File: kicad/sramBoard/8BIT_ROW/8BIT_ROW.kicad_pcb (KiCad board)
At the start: 4 copper layers, 64 parts, among them Q1 NMOS, Q10 NMOS, Q11 PMOS, Q12 NMOS, Q13 PMOS, Q14 NMOS, Q15 NMOS, Q16 NMOS, Q17 NMOS, Q18 NMOS, Q19 PMOS, Q2 NMOS, Q20 NMOS, Q21 PMOS, Q22 NMOS, Q23 NMOS, Q24 NMOS, Q25 NMOS, Q26 NMOS, Q27 PMOS, Q28 NMOS, Q29 PMOS, Q3 PMOS, Q30 NMOS, Q31 NMOS, Q32 NMOS, Q33 NMOS, Q34 NMOS, Q35 PMOS, Q36 NMOS, Q37 PMOS, Q38 NMOS, Q39 NMOS, Q4 NMOS, Q40 NMOS, Q41 NMOS, Q42 NMOS, Q43 PMOS, Q44 NMOS, Q45 PMOS, Q46 NMOS, Q47 NMOS, Q48 NMOS, Q49 NMOS, Q5 PMOS, Q50 NMOS, Q51 PMOS, Q52 NMOS, Q53 PMOS, Q54 NMOS, Q55 NMOS, Q56 NMOS, Q57 NMOS, Q58 NMOS, Q59 PMOS, Q6 NMOS, Q60 NMOS, Q61 PMOS, Q62 NMOS, Q63 NMOS, Q64 NMOS, Q7 NMOS, Q8 NMOS, Q9 NMOS

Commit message: added busbars but still some issues
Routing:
- added copper zone on B.Cu, net /BL_{0}
- added copper zone on B.Cu, net /BL_{1}
- added copper zone on B.Cu, net /BL_{2}
- added copper zone on B.Cu, net /BL_{3}
- added copper zone on B.Cu, net /BL_{4}
- added copper zone on B.Cu, net /BL_{5}
- added copper zone on B.Cu, net /BL_{6}
- added copper zone on B.Cu, net /BL_{7}
- added copper zone on B.Cu, net /~{BL_{0}}
- added copper zone on B.Cu, net /~{BL_{1}}
- added copper zone on B.Cu, net /~{BL_{2}}
- added copper zone on B.Cu, net /~{BL_{3}}
- added copper zone on B.Cu, net /~{BL_{4}}
- added copper zone on B.Cu, net /~{BL_{5}}
- added copper zone on B.Cu, net /~{BL_{6}}
- added copper zone on B.Cu, net /~{BL_{7}}

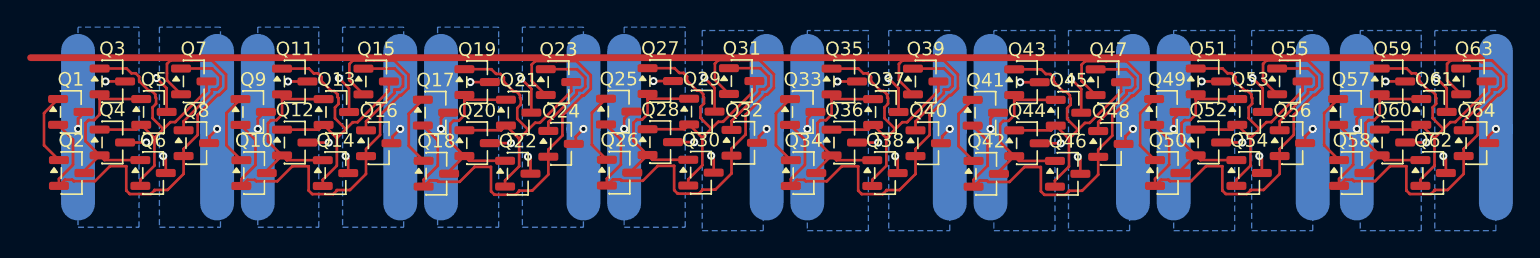
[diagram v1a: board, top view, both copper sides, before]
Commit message: add pmos resistors
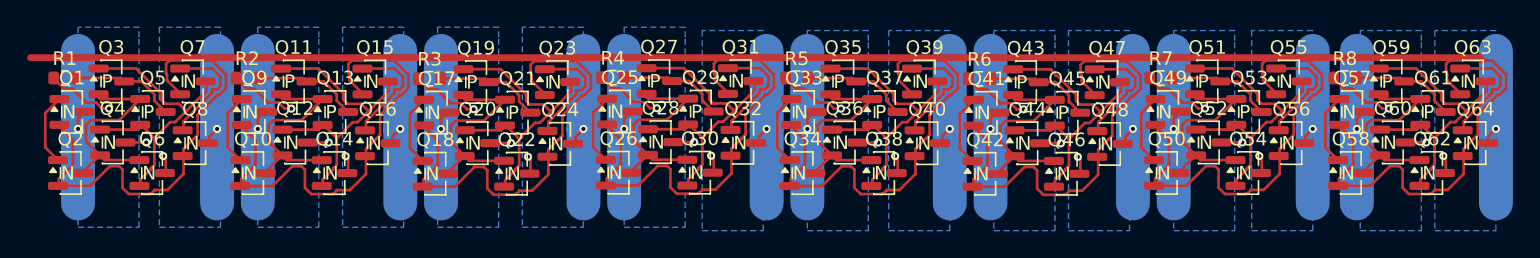
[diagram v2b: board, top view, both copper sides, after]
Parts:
- added R1: 47R, Resistor_SMD:R_0603_1608Metric, F.Cu at (88.5, 37.8)
- added R2: 47R, Resistor_SMD:R_0603_1608Metric, F.Cu at (102.0, 37.8)
- added R3: 47R, Resistor_SMD:R_0603_1608Metric, F.Cu at (115.4, 37.8)
- added R4: 47R, Resistor_SMD:R_0603_1608Metric, F.Cu at (128.9, 37.7)
- added R5: 47R, Resistor_SMD:R_0603_1608Metric, F.Cu at (142.5, 37.8)
- added R6: 47R, Resistor_SMD:R_0603_1608Metric, F.Cu at (155.9, 37.8)
- added R7: 47R, Resistor_SMD:R_0603_1608Metric, F.Cu at (169.3, 37.8)
- added R8: 47R, Resistor_SMD:R_0603_1608Metric, F.Cu at (182.9, 37.8)
- Q1, Q10, Q12, Q14, Q15, Q16, Q17, Q18, Q2, Q20, Q22, Q23, Q24, Q25, Q26, Q28, Q30, Q31, Q32, Q33, Q34, Q36, Q38, Q39, Q4, Q40, Q41, Q42, Q44, Q46, Q47, Q48, Q49, Q50, Q52, Q54, Q55, Q56, Q57, Q58, Q6, Q60, Q62, Q63, Q64, Q7, Q8, Q9: footprint Package_TO_SOT_SMD:SOT-23 -> easyeda2kicad:SOT-23-N
- Q11, Q13, Q19, Q21, Q27, Q29, Q3, Q35, Q37, Q43, Q45, Q5, Q51, Q53, Q59, Q61: footprint Package_TO_SOT_SMD:SOT-23 -> easyeda2kicad:SOT-23-P
- moved Q17 0.16 mm to (116.0, 40.3)
- moved Q9 0.16 mm to (102.6, 40.3)
- moved Q1 0.16 mm to (89.1, 40.2)
- moved Q25 0.16 mm to (129.5, 40.2)
- moved Q33 0.16 mm to (143.1, 40.3)
- moved Q41 0.16 mm to (156.5, 40.3)
- moved Q49 0.16 mm to (169.9, 40.2)
- moved Q57 0.16 mm to (183.5, 40.2)
- moved Q12 0.10 mm to (105.6, 42.5)
- moved Q20 0.10 mm to (119.0, 42.5)
- moved Q28 0.10 mm to (132.5, 42.5)
- moved Q36 0.10 mm to (146.1, 42.5)
- moved Q4 0.10 mm to (92.1, 42.5)
- moved Q44 0.10 mm to (159.5, 42.6)
- moved Q52 0.10 mm to (172.9, 42.5)
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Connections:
- Q11 pad 3: +5V -> Net-(Q11-S)
- Q13 pad 3: +5V -> Net-(Q11-S)
- Q19 pad 3: +5V -> Net-(Q19-S)
- Q21 pad 3: +5V -> Net-(Q19-S)
- Q27 pad 3: +5V -> Net-(Q27-S)
- Q29 pad 3: +5V -> Net-(Q27-S)
- Q3 pad 3: +5V -> Net-(Q3-S)
- Q35 pad 3: +5V -> Net-(Q35-S)
- Q37 pad 3: +5V -> Net-(Q35-S)
- Q43 pad 3: +5V -> Net-(Q43-S)
- Q45 pad 3: +5V -> Net-(Q43-S)
- Q5 pad 3: +5V -> Net-(Q3-S)
- Q51 pad 3: +5V -> Net-(Q51-S)
- Q53 pad 3: +5V -> Net-(Q51-S)
- Q59 pad 3: +5V -> Net-(Q59-S)
- Q61 pad 3: +5V -> Net-(Q59-S)
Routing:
- net Net-(Q51-S): track 0.00 -> 7.91 mm
- net Net-(Q43-S): track 0.00 -> 7.91 mm
- net Net-(Q59-S): track 0.00 -> 7.91 mm
- net Net-(Q3-S): track 0.00 -> 7.91 mm
- net Net-(Q19-S): track 0.00 -> 7.91 mm
- net Net-(Q11-S): track 0.00 -> 7.91 mm
- net Net-(Q35-S): track 0.00 -> 7.91 mm
- net Net-(Q27-S): track 0.00 -> 7.91 mm
- net +5V: track 34.0 -> 40.1 mm, vias 16 -> 8
- net Net-(Q58-S): track 13.6 -> 15.8 mm
- net Net-(Q2-S): track 13.6 -> 15.8 mm
- net Net-(Q50-S): track 13.6 -> 15.8 mm
- net Net-(Q42-S): track 13.6 -> 15.8 mm
- net Net-(Q34-S): track 13.6 -> 15.8 mm
- net Net-(Q10-S): track 13.6 -> 15.8 mm
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
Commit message: finish main pcb
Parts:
- added D1: LED, LED_SMD:LED_0805_2012Metric_Pad1.15x1.40mm_HandSolder, B.Cu at (95.3, 41.0)
- added D2: LED, LED_SMD:LED_0805_2012Metric_Pad1.15x1.40mm_HandSolder, B.Cu at (108.7, 41.0)
- added D3: LED, LED_SMD:LED_0805_2012Metric_Pad1.15x1.40mm_HandSolder, B.Cu at (122.2, 41.0)
- added D4: LED, LED_SMD:LED_0805_2012Metric_Pad1.15x1.40mm_HandSolder, B.Cu at (135.7, 41.0)
- added D5: LED, LED_SMD:LED_0805_2012Metric_Pad1.15x1.40mm_HandSolder, B.Cu at (149.2, 41.0)
- added D6: LED, LED_SMD:LED_0805_2012Metric_Pad1.15x1.40mm_HandSolder, B.Cu at (162.7, 41.1)
- added D7: LED, LED_SMD:LED_0805_2012Metric_Pad1.15x1.40mm_HandSolder, B.Cu at (176.1, 41.0)
- added D8: LED, LED_SMD:LED_0805_2012Metric_Pad1.15x1.40mm_HandSolder, B.Cu at (189.6, 41.0)
- added Q14: NMOS, easyeda2kicad:SOT-23-N, B.Cu at (106.5, 38.0)
- added Q23: NMOS, easyeda2kicad:SOT-23-N, B.Cu at (119.9, 38.0)
- added Q32: NMOS, easyeda2kicad:SOT-23-N, B.Cu at (133.4, 38.0)
- added Q41: NMOS, easyeda2kicad:SOT-23-N, B.Cu at (147.0, 38.0)
- added Q5: NMOS, easyeda2kicad:SOT-23-N, B.Cu at (93.0, 38.0)
- added Q50: NMOS, easyeda2kicad:SOT-23-N, B.Cu at (160.4, 38.1)
- added Q59: NMOS, easyeda2kicad:SOT-23-N, B.Cu at (173.8, 38.0)
- added Q68: NMOS, easyeda2kicad:SOT-23-N, B.Cu at (187.4, 38.0)
- added R1: 220R, Resistor_SMD:R_0603_1608Metric_Pad0.98x0.95mm_HandSolder, B.Cu at (95.8, 38.2)
- added R11: 220R, Resistor_SMD:R_0603_1608Metric_Pad0.98x0.95mm_HandSolder, B.Cu at (163.2, 38.3)
- added R13: 220R, Resistor_SMD:R_0603_1608Metric_Pad0.98x0.95mm_HandSolder, B.Cu at (176.6, 38.2)
- added R15: 220R, Resistor_SMD:R_0603_1608Metric_Pad0.98x0.95mm_HandSolder, B.Cu at (190.1, 38.2)
- added R3: 220R, Resistor_SMD:R_0603_1608Metric_Pad0.98x0.95mm_HandSolder, B.Cu at (109.2, 38.3)
- added R5: 220R, Resistor_SMD:R_0603_1608Metric_Pad0.98x0.95mm_HandSolder, B.Cu at (122.7, 38.3)
- added R7: 220R, Resistor_SMD:R_0603_1608Metric_Pad0.98x0.95mm_HandSolder, B.Cu at (136.2, 38.2)
- added R9: 220R, Resistor_SMD:R_0603_1608Metric_Pad0.98x0.95mm_HandSolder, B.Cu at (149.7, 38.3)
- renumbered Q9 to Q10, Q10 to Q11, Q11 to Q12, Q12 to Q13, Q13 to Q15, Q14 to Q16, Q15 to Q17, Q16 to Q18, Q17 to Q19, Q18 to Q20, Q19 to Q21, Q20 to Q22, Q21 to Q24, Q22 to Q25, Q23 to Q26, Q24 to Q27, Q25 to Q28, Q26 to Q29, Q27 to Q30, Q28 to Q31, Q29 to Q33, Q30 to Q34, Q31 to Q35, Q32 to Q36, Q33 to Q37, Q34 to Q38, Q35 to Q39, Q36 to Q40, Q37 to Q42, Q38 to Q43, Q39 to Q44, Q40 to Q45, Q41 to Q46, Q42 to Q47, Q43 to Q48, Q44 to Q49, Q45 to Q51, Q46 to Q52, Q47 to Q53, Q48 to Q54, Q49 to Q55, Q50 to Q56, Q51 to Q57, Q52 to Q58, Q5 to Q6, Q53 to Q60, Q54 to Q61, Q55 to Q62, Q56 to Q63, Q57 to Q64, Q58 to Q65, Q59 to Q66, Q60 to Q67, Q61 to Q69, Q6 to Q7, Q62 to Q70, Q63 to Q71, Q64 to Q72, Q7 to Q8, Q8 to Q9, R5 to R10, R6 to R12, R7 to R14, R8 to R16, R1 to R2, R2 to R4, R3 to R6, R4 to R8
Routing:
- net GND: track 23.1 -> 42.3 mm
- net +5V: track 40.1 -> 50.9 mm
- net Net-(Q65-S): track 15.8 -> 19.4 mm, vias 0 -> 1
- net Net-(Q56-S): track 15.8 -> 19.4 mm, vias 0 -> 1
- net Net-(Q38-S): track 15.8 -> 19.4 mm, vias 0 -> 1
- net Net-(Q29-S): track 15.8 -> 19.4 mm, vias 0 -> 1
- net Net-(Q11-S): track 15.8 -> 19.4 mm, vias 0 -> 1
- net Net-(Q47-S): track 15.8 -> 19.4 mm, vias 0 -> 1
- net Net-(Q20-S): track 15.8 -> 19.4 mm, vias 0 -> 1
- net Net-(Q2-S): track 15.8 -> 19.4 mm, vias 0 -> 1
- net Net-(D6-A): track 0.00 -> 2.47 mm
- net Net-(D8-A): track 0.00 -> 2.47 mm
- net Net-(D7-A): track 0.00 -> 2.47 mm
- net Net-(D5-A): track 0.00 -> 2.47 mm
- net Net-(D4-A): track 0.00 -> 2.47 mm
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
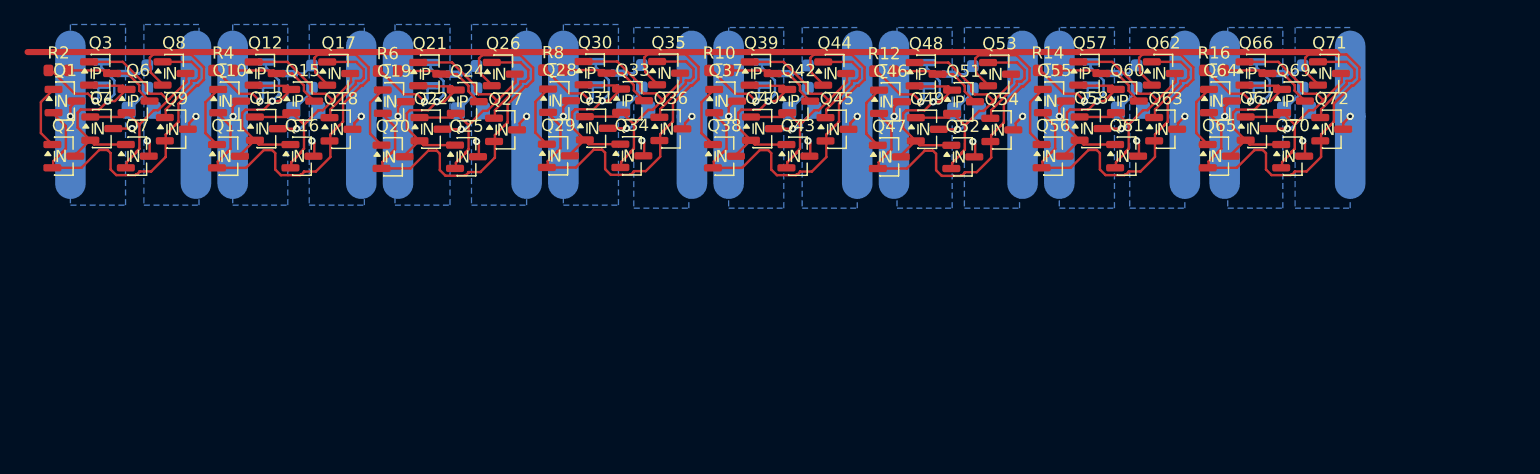
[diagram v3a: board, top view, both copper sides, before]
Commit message: fix main ram board
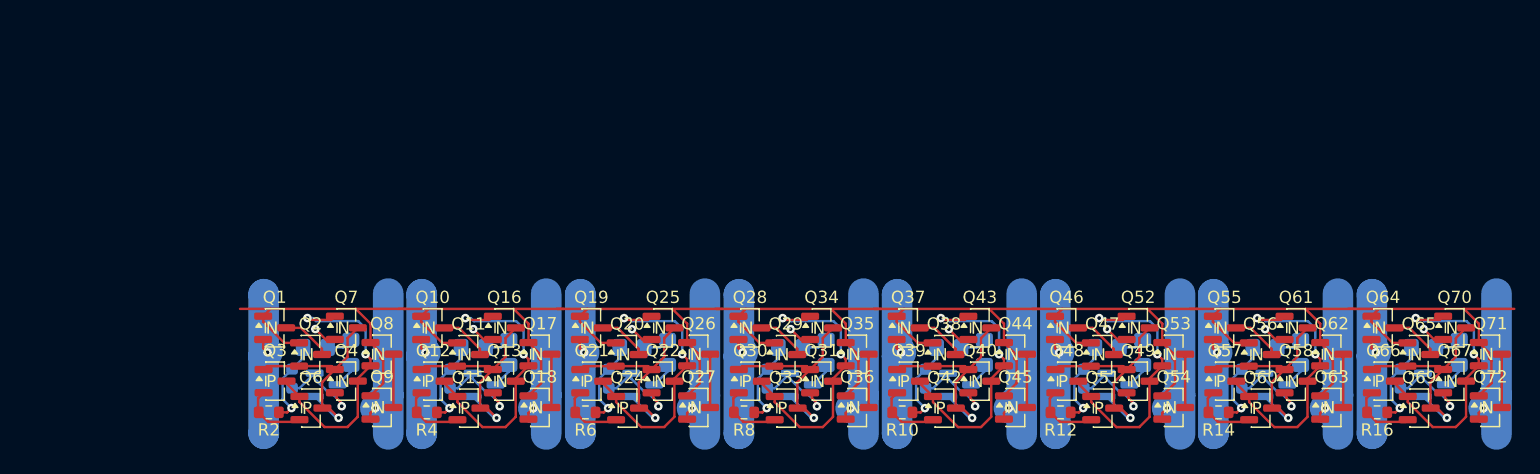
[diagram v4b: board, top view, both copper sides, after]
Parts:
- added C1: 100nC, Capacitor_SMD:C_0603_1608Metric, B.Cu at (107.6, 62.9)
- added C2: 100nC, Capacitor_SMD:C_0603_1608Metric, B.Cu at (120.5, 62.9)
- added C3: 100nC, Capacitor_SMD:C_0603_1608Metric, B.Cu at (133.5, 62.9)
- added C4: 100nC, Capacitor_SMD:C_0603_1608Metric, B.Cu at (146.4, 62.9)
- added C5: 100nC, Capacitor_SMD:C_0603_1608Metric, B.Cu at (159.3, 62.9)
- added C6: 100nC, Capacitor_SMD:C_0603_1608Metric, B.Cu at (172.3, 62.9)
- added C7: 100nC, Capacitor_SMD:C_0603_1608Metric, B.Cu at (185.2, 62.9)
- added C8: 100nC, Capacitor_SMD:C_0603_1608Metric, B.Cu at (198.1, 62.9)
- Q1, Q10, Q11, Q13, Q14, Q16, Q17, Q18, Q19, Q2, Q20, Q22, Q23, Q25, Q26, Q27, Q28, Q29, Q31, Q32, Q34, Q35, Q36, Q37, Q38, Q4, Q40, Q41, Q43, Q44, Q45, Q46, Q47, Q49, Q5, Q50, Q52, Q53, Q54, Q55, Q56, Q58, Q59, Q61, Q62, Q63, Q64, Q65, Q67, Q68, Q7, Q70, Q71, Q72, Q8, Q9: value NMOS -> Q_NMOS_GSD
- Q12, Q15, Q21, Q24, Q3, Q30, Q33, Q39, Q42, Q48, Q51, Q57, Q6, Q60, Q66, Q69: value PMOS -> Q_PMOS_GSD
- R1, R11, R13, R15, R3, R5, R7, R9: value 220R -> 470R; footprint Resistor_SMD:R_0603_1608Metric_Pad0.98x0.95mm_HandSolder -> Resistor_SMD:R_0805_2012Metric_Pad1.20x1.40mm_HandSolder
- moved R2 32.8 mm to (105.7, 65.7), turned to 180 degrees
- moved R4 32.5 mm to (118.6, 65.7), turned to 180 degrees
- moved R6 32.2 mm to (131.6, 65.7), turned to 180 degrees
- moved R8 32.0 mm to (144.5, 65.7), turned to 180 degrees
- moved R10 31.7 mm to (157.4, 65.7), turned to 180 degrees
- moved R12 31.4 mm to (170.4, 65.7), turned to 180 degrees
- moved R14 31.2 mm to (183.2, 65.7), turned to 180 degrees
- moved R16 30.9 mm to (196.2, 65.7), turned to 180 degrees
- moved Q5 30.8 mm to (110.5, 63.4)
- moved Q14 30.5 mm to (123.3, 63.4)
- moved Q23 30.2 mm to (136.3, 63.4)
- moved Q32 30.0 mm to (149.3, 63.4)
- moved Q41 29.6 mm to (162.2, 63.4)
- moved Q50 29.3 mm to (175.1, 63.4)
- moved Q59 29.1 mm to (188.0, 63.4)
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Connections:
- D1 pad 1: GND -> Net-(D1-K)
- D2 pad 1: GND -> Net-(D2-K)
- D3 pad 1: GND -> Net-(D3-K)
- D4 pad 1: GND -> Net-(D4-K)
- D5 pad 1: GND -> Net-(D5-K)
- D6 pad 1: GND -> Net-(D6-K)
- D7 pad 1: GND -> Net-(D7-K)
- D8 pad 1: GND -> Net-(D8-K)
- Q1 pad 1: Net-(Q1-D) -> /WL
- Q1 pad 2: /WL -> /BL_{0}
- Q1 pad 3: /BL_{0} -> Net-(Q1-D)
- Q10 pad 1: Net-(Q10-D) -> /WL
- Q10 pad 2: /WL -> /BL_{1}
- Q10 pad 3: /BL_{1} -> Net-(Q10-D)
- Q11 pad 1: Net-(Q10-D) -> /WL
- Q11 pad 2: /WL -> Net-(Q11-S)
- Q11 pad 3: Net-(Q11-S) -> Net-(Q10-D)
- Q12 pad 1: Net-(Q12-D) -> Net-(Q11-S)
- Q12 pad 2: Net-(Q11-S) -> Net-(Q12-S)
- Q12 pad 3: Net-(Q12-S) -> Net-(Q12-D)
- Q13 pad 1: Net-(Q12-D) -> Net-(Q11-S)
- Q13 pad 2: Net-(Q11-S) -> GND
- Q13 pad 3: GND -> Net-(Q12-D)
- Q14 pad 1: +5V -> Net-(Q11-S)
- Q14 pad 2: Net-(Q11-S) -> GND
- Q14 pad 3: Net-(Q14-S) -> Net-(D2-K)
- Q15 pad 1: Net-(Q11-S) -> Net-(Q12-D)
- Q15 pad 2: Net-(Q12-D) -> Net-(Q12-S)
- Q15 pad 3: Net-(Q12-S) -> Net-(Q11-S)
- Q16 pad 1: Net-(Q11-S) -> Net-(Q12-D)
- Q16 pad 2: Net-(Q12-D) -> GND
- Q16 pad 3: GND -> Net-(Q11-S)
- Q17 pad 1: Net-(Q17-D) -> /WL
- Q17 pad 2: /WL -> Net-(Q12-D)
- Q17 pad 3: Net-(Q12-D) -> Net-(Q17-D)
- Q18 pad 1: Net-(Q17-D) -> /WL
- Q18 pad 2: /WL -> /~{BL_{1}}
- Q18 pad 3: /~{BL_{1}} -> Net-(Q17-D)
- Q19 pad 1: Net-(Q19-D) -> /WL
- Q19 pad 2: /WL -> /BL_{2}
- Q19 pad 3: /BL_{2} -> Net-(Q19-D)
- Q2 pad 1: Net-(Q1-D) -> /WL
- Q2 pad 2: /WL -> Net-(Q2-S)
- Q2 pad 3: Net-(Q2-S) -> Net-(Q1-D)
- Q20 pad 1: Net-(Q19-D) -> /WL
- Q20 pad 2: /WL -> Net-(Q20-S)
- Q20 pad 3: Net-(Q20-S) -> Net-(Q19-D)
- Q21 pad 1: Net-(Q21-D) -> Net-(Q20-S)
- Q21 pad 2: Net-(Q20-S) -> Net-(Q21-S)
- Q21 pad 3: Net-(Q21-S) -> Net-(Q21-D)
- Q22 pad 1: Net-(Q21-D) -> Net-(Q20-S)
- Q22 pad 2: Net-(Q20-S) -> GND
- Q22 pad 3: GND -> Net-(Q21-D)
- Q23 pad 1: +5V -> Net-(Q20-S)
- Q23 pad 2: Net-(Q20-S) -> GND
- Q23 pad 3: Net-(Q23-S) -> Net-(D3-K)
- Q24 pad 1: Net-(Q20-S) -> Net-(Q21-D)
- Q24 pad 2: Net-(Q21-D) -> Net-(Q21-S)
- Q24 pad 3: Net-(Q21-S) -> Net-(Q20-S)
- Q25 pad 1: Net-(Q20-S) -> Net-(Q21-D)
- Q25 pad 2: Net-(Q21-D) -> GND
- Q25 pad 3: GND -> Net-(Q20-S)
- Q26 pad 1: Net-(Q26-D) -> /WL
- Q26 pad 2: /WL -> Net-(Q21-D)
- Q26 pad 3: Net-(Q21-D) -> Net-(Q26-D)
- Q27 pad 1: Net-(Q26-D) -> /WL
- Q27 pad 2: /WL -> /~{BL_{2}}
- Q27 pad 3: /~{BL_{2}} -> Net-(Q26-D)
- Q28 pad 1: Net-(Q28-D) -> /WL
- Q28 pad 2: /WL -> /BL_{3}
- Q28 pad 3: /BL_{3} -> Net-(Q28-D)
- Q29 pad 1: Net-(Q28-D) -> /WL
- Q29 pad 2: /WL -> Net-(Q29-S)
- Q29 pad 3: Net-(Q29-S) -> Net-(Q28-D)
- Q3 pad 1: Net-(Q3-D) -> Net-(Q2-S)
- Q3 pad 2: Net-(Q2-S) -> Net-(Q3-S)
- Q3 pad 3: Net-(Q3-S) -> Net-(Q3-D)
- Q30 pad 1: Net-(Q30-D) -> Net-(Q29-S)
- Q30 pad 2: Net-(Q29-S) -> Net-(Q30-S)
- Q30 pad 3: Net-(Q30-S) -> Net-(Q30-D)
- Q31 pad 1: Net-(Q30-D) -> Net-(Q29-S)
- Q31 pad 2: Net-(Q29-S) -> GND
- Q31 pad 3: GND -> Net-(Q30-D)
- Q32 pad 1: +5V -> Net-(Q29-S)
- Q32 pad 2: Net-(Q29-S) -> GND
- Q32 pad 3: Net-(Q32-S) -> Net-(D4-K)
- Q33 pad 1: Net-(Q29-S) -> Net-(Q30-D)
- Q33 pad 2: Net-(Q30-D) -> Net-(Q30-S)
- Q33 pad 3: Net-(Q30-S) -> Net-(Q29-S)
- Q34 pad 1: Net-(Q29-S) -> Net-(Q30-D)
- Q34 pad 2: Net-(Q30-D) -> GND
- Q34 pad 3: GND -> Net-(Q29-S)
- Q35 pad 1: Net-(Q35-D) -> /WL
- Q35 pad 2: /WL -> Net-(Q30-D)
- Q35 pad 3: Net-(Q30-D) -> Net-(Q35-D)
- Q36 pad 1: Net-(Q35-D) -> /WL
- Q36 pad 2: /WL -> /~{BL_{3}}
- Q36 pad 3: /~{BL_{3}} -> Net-(Q35-D)
- Q37 pad 1: Net-(Q37-D) -> /WL
- Q37 pad 2: /WL -> /BL_{4}
- Q37 pad 3: /BL_{4} -> Net-(Q37-D)
- Q38 pad 1: Net-(Q37-D) -> /WL
- Q38 pad 2: /WL -> Net-(Q38-S)
- Q38 pad 3: Net-(Q38-S) -> Net-(Q37-D)
- Q39 pad 1: Net-(Q39-D) -> Net-(Q38-S)
- Q39 pad 2: Net-(Q38-S) -> Net-(Q39-S)
- Q39 pad 3: Net-(Q39-S) -> Net-(Q39-D)
- Q4 pad 1: Net-(Q3-D) -> Net-(Q2-S)
- Q4 pad 2: Net-(Q2-S) -> GND
- Q4 pad 3: GND -> Net-(Q3-D)
- Q40 pad 1: Net-(Q39-D) -> Net-(Q38-S)
- Q40 pad 2: Net-(Q38-S) -> GND
- Q40 pad 3: GND -> Net-(Q39-D)
- Q41 pad 1: +5V -> Net-(Q38-S)
- Q41 pad 2: Net-(Q38-S) -> GND
- Q41 pad 3: Net-(Q41-S) -> Net-(D5-K)
- Q42 pad 1: Net-(Q38-S) -> Net-(Q39-D)
- Q42 pad 2: Net-(Q39-D) -> Net-(Q39-S)
- Q42 pad 3: Net-(Q39-S) -> Net-(Q38-S)
- Q43 pad 1: Net-(Q38-S) -> Net-(Q39-D)
- Q43 pad 2: Net-(Q39-D) -> GND
- Q43 pad 3: GND -> Net-(Q38-S)
- Q44 pad 1: Net-(Q44-D) -> /WL
- Q44 pad 2: /WL -> Net-(Q39-D)
- Q44 pad 3: Net-(Q39-D) -> Net-(Q44-D)
- Q45 pad 1: Net-(Q44-D) -> /WL
- Q45 pad 2: /WL -> /~{BL_{4}}
- Q45 pad 3: /~{BL_{4}} -> Net-(Q44-D)
- Q46 pad 1: Net-(Q46-D) -> /WL
- Q46 pad 2: /WL -> /BL_{5}
- Q46 pad 3: /BL_{5} -> Net-(Q46-D)
- Q47 pad 1: Net-(Q46-D) -> /WL
- Q47 pad 2: /WL -> Net-(Q47-S)
- Q47 pad 3: Net-(Q47-S) -> Net-(Q46-D)
- Q48 pad 1: Net-(Q48-D) -> Net-(Q47-S)
- Q48 pad 2: Net-(Q47-S) -> Net-(Q48-S)
- Q48 pad 3: Net-(Q48-S) -> Net-(Q48-D)
- Q49 pad 1: Net-(Q48-D) -> Net-(Q47-S)
- Q49 pad 2: Net-(Q47-S) -> GND
- Q49 pad 3: GND -> Net-(Q48-D)
- Q5 pad 1: +5V -> Net-(Q2-S)
- Q5 pad 2: Net-(Q2-S) -> GND
- Q5 pad 3: Net-(Q5-S) -> Net-(D1-K)
- Q50 pad 1: +5V -> Net-(Q47-S)
- Q50 pad 2: Net-(Q47-S) -> GND
- Q50 pad 3: Net-(Q50-S) -> Net-(D6-K)
- Q51 pad 1: Net-(Q47-S) -> Net-(Q48-D)
- Q51 pad 2: Net-(Q48-D) -> Net-(Q48-S)
- Q51 pad 3: Net-(Q48-S) -> Net-(Q47-S)
- Q52 pad 1: Net-(Q47-S) -> Net-(Q48-D)
- Q52 pad 2: Net-(Q48-D) -> GND
- Q52 pad 3: GND -> Net-(Q47-S)
- Q53 pad 1: Net-(Q53-D) -> /WL
- Q53 pad 2: /WL -> Net-(Q48-D)
- Q53 pad 3: Net-(Q48-D) -> Net-(Q53-D)
- Q54 pad 1: Net-(Q53-D) -> /WL
- Q54 pad 2: /WL -> /~{BL_{5}}
- Q54 pad 3: /~{BL_{5}} -> Net-(Q53-D)
- Q55 pad 1: Net-(Q55-D) -> /WL
- Q55 pad 2: /WL -> /BL_{6}
- Q55 pad 3: /BL_{6} -> Net-(Q55-D)
- Q56 pad 1: Net-(Q55-D) -> /WL
- Q56 pad 2: /WL -> Net-(Q56-S)
- Q56 pad 3: Net-(Q56-S) -> Net-(Q55-D)
- Q57 pad 1: Net-(Q57-D) -> Net-(Q56-S)
- Q57 pad 2: Net-(Q56-S) -> Net-(Q57-S)
- Q57 pad 3: Net-(Q57-S) -> Net-(Q57-D)
- Q58 pad 1: Net-(Q57-D) -> Net-(Q56-S)
- Q58 pad 2: Net-(Q56-S) -> GND
- Q58 pad 3: GND -> Net-(Q57-D)
- Q59 pad 1: +5V -> Net-(Q56-S)
- Q59 pad 2: Net-(Q56-S) -> GND
- Q59 pad 3: Net-(Q59-S) -> Net-(D7-K)
- Q6 pad 1: Net-(Q2-S) -> Net-(Q3-D)
- Q6 pad 2: Net-(Q3-D) -> Net-(Q3-S)
- Q6 pad 3: Net-(Q3-S) -> Net-(Q2-S)
- Q60 pad 1: Net-(Q56-S) -> Net-(Q57-D)
- Q60 pad 2: Net-(Q57-D) -> Net-(Q57-S)
- Q60 pad 3: Net-(Q57-S) -> Net-(Q56-S)
- Q61 pad 1: Net-(Q56-S) -> Net-(Q57-D)
- Q61 pad 2: Net-(Q57-D) -> GND
- Q61 pad 3: GND -> Net-(Q56-S)
- Q62 pad 1: Net-(Q62-D) -> /WL
- Q62 pad 2: /WL -> Net-(Q57-D)
- Q62 pad 3: Net-(Q57-D) -> Net-(Q62-D)
- Q63 pad 1: Net-(Q62-D) -> /WL
- Q63 pad 2: /WL -> /~{BL_{6}}
- Q63 pad 3: /~{BL_{6}} -> Net-(Q62-D)
- Q64 pad 1: Net-(Q64-D) -> /WL
- Q64 pad 2: /WL -> /BL_{7}
- Q64 pad 3: /BL_{7} -> Net-(Q64-D)
- Q65 pad 1: Net-(Q64-D) -> /WL
- Q65 pad 2: /WL -> Net-(Q65-S)
- Q65 pad 3: Net-(Q65-S) -> Net-(Q64-D)
- Q66 pad 1: Net-(Q66-D) -> Net-(Q65-S)
- Q66 pad 2: Net-(Q65-S) -> Net-(Q66-S)
- Q66 pad 3: Net-(Q66-S) -> Net-(Q66-D)
- Q67 pad 1: Net-(Q66-D) -> Net-(Q65-S)
- Q67 pad 2: Net-(Q65-S) -> GND
- Q67 pad 3: GND -> Net-(Q66-D)
- Q68 pad 1: +5V -> Net-(Q65-S)
- Q68 pad 2: Net-(Q65-S) -> GND
- Q68 pad 3: Net-(Q68-S) -> Net-(D8-K)
- Q69 pad 1: Net-(Q65-S) -> Net-(Q66-D)
- Q69 pad 2: Net-(Q66-D) -> Net-(Q66-S)
- Q69 pad 3: Net-(Q66-S) -> Net-(Q65-S)
- Q7 pad 1: Net-(Q2-S) -> Net-(Q3-D)
- Q7 pad 2: Net-(Q3-D) -> GND
- Q7 pad 3: GND -> Net-(Q2-S)
- Q70 pad 1: Net-(Q65-S) -> Net-(Q66-D)
- Q70 pad 2: Net-(Q66-D) -> GND
- Q70 pad 3: GND -> Net-(Q65-S)
- Q71 pad 1: Net-(Q71-D) -> /WL
- Q71 pad 2: /WL -> Net-(Q66-D)
- Q71 pad 3: Net-(Q66-D) -> Net-(Q71-D)
- Q72 pad 1: Net-(Q71-D) -> /WL
- Q72 pad 2: /WL -> /~{BL_{7}}
- Q72 pad 3: /~{BL_{7}} -> Net-(Q71-D)
- Q8 pad 1: Net-(Q8-D) -> /WL
- Q8 pad 2: /WL -> Net-(Q3-D)
- Q8 pad 3: Net-(Q3-D) -> Net-(Q8-D)
- Q9 pad 1: Net-(Q8-D) -> /WL
- Q9 pad 2: /WL -> /~{BL_{0}}
- Q9 pad 3: /~{BL_{0}} -> Net-(Q8-D)
- R1 pad 1: Net-(Q5-S) -> +5V
- R11 pad 1: Net-(Q50-S) -> +5V
- R13 pad 1: Net-(Q59-S) -> +5V
- R15 pad 1: Net-(Q68-S) -> +5V
- R3 pad 1: Net-(Q14-S) -> +5V
- R5 pad 1: Net-(Q23-S) -> +5V
- R7 pad 1: Net-(Q32-S) -> +5V
- R9 pad 1: Net-(Q41-S) -> +5V
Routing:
- net /WL: track 378.9 -> 215.6 mm
- net GND: track 42.3 -> 75.6 mm
- net +5V: track 50.9 -> 58.9 mm
- net Net-(Q17-D): track 8.46 -> 4.35 mm
- net Net-(Q71-D): track 8.46 -> 4.35 mm
- net Net-(Q26-D): track 8.46 -> 4.35 mm
- net Net-(Q8-D): track 8.46 -> 4.35 mm
- net Net-(Q62-D): track 8.46 -> 4.35 mm
- net Net-(Q44-D): track 8.46 -> 4.35 mm
- net Net-(Q35-D): track 8.46 -> 4.35 mm
- net Net-(Q53-D): track 8.46 -> 4.35 mm
- net Net-(Q57-S): track 7.91 -> 5.50 mm
- net Net-(Q48-S): track 7.91 -> 5.50 mm
- net Net-(Q12-S): track 7.91 -> 5.50 mm
- net Net-(Q21-S): track 7.91 -> 5.50 mm
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- removed copper zone on B.Cu, net /BL_{0}
- removed copper zone on B.Cu, net /BL_{1}
- removed copper zone on B.Cu, net /BL_{2}
- removed copper zone on B.Cu, net /BL_{3}
- removed copper zone on B.Cu, net /BL_{4}
- removed copper zone on B.Cu, net /BL_{5}
- removed copper zone on B.Cu, net /BL_{6}
- removed copper zone on B.Cu, net /BL_{7}
- removed copper zone on B.Cu, net /~{BL_{0}}
- removed copper zone on B.Cu, net /~{BL_{1}}
- removed copper zone on B.Cu, net /~{BL_{2}}
- removed copper zone on B.Cu, net /~{BL_{3}}
- removed copper zone on B.Cu, net /~{BL_{4}}
- removed copper zone on B.Cu, net /~{BL_{5}}
- removed copper zone on B.Cu, net /~{BL_{6}}
- removed copper zone on B.Cu, net /~{BL_{7}}

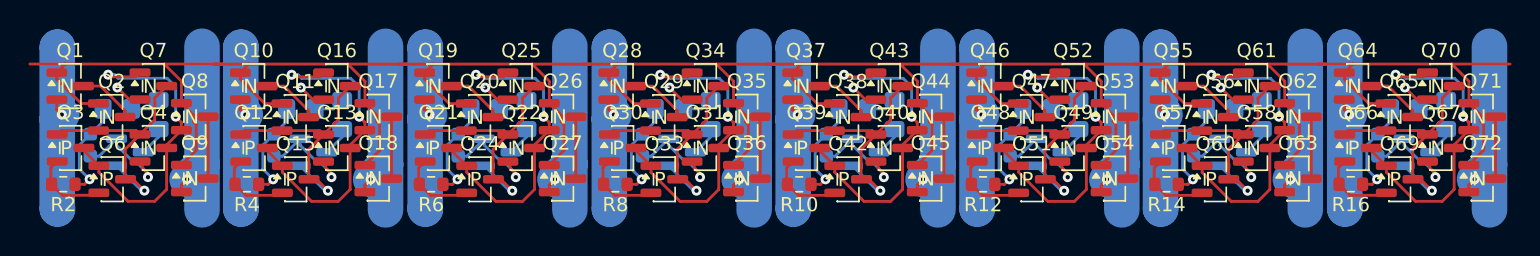
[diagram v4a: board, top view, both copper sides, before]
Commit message: Add breakout board through holes on main ram board
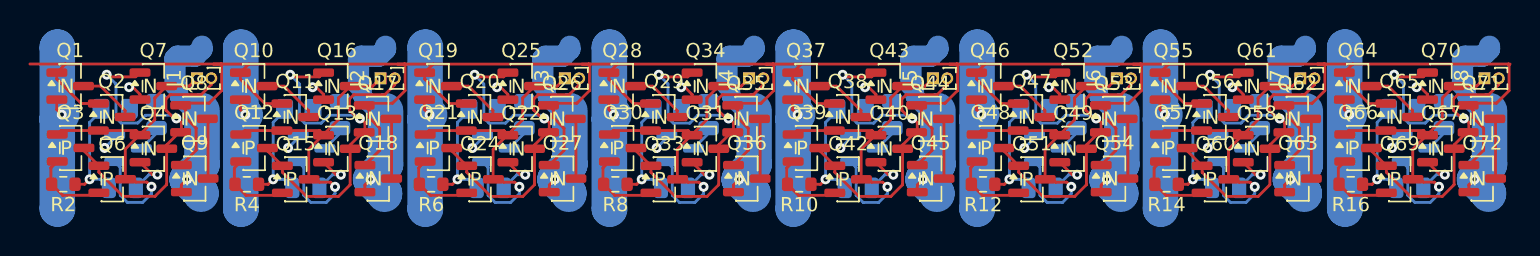
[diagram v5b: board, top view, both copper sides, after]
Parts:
- added J1: Conn_01x02_Pin, Connector_PinHeader_1.00mm:PinHeader_1x02_P1.00mm_Vertical, F.Cu at (115.1, 58.2)
- added J2: Conn_01x02_Pin, Connector_PinHeader_1.00mm:PinHeader_1x02_P1.00mm_Vertical, F.Cu at (128.0, 58.2)
- added J3: Conn_01x02_Pin, Connector_PinHeader_1.00mm:PinHeader_1x02_P1.00mm_Vertical, F.Cu at (141.0, 58.2)
- added J4: Conn_01x02_Pin, Connector_PinHeader_1.00mm:PinHeader_1x02_P1.00mm_Vertical, F.Cu at (153.9, 58.2)
- added J5: Conn_01x02_Pin, Connector_PinHeader_1.00mm:PinHeader_1x02_P1.00mm_Vertical, F.Cu at (166.8, 58.2)
- added J6: Conn_01x02_Pin, Connector_PinHeader_1.00mm:PinHeader_1x02_P1.00mm_Vertical, F.Cu at (179.8, 58.2)
- added J7: Conn_01x02_Pin, Connector_PinHeader_1.00mm:PinHeader_1x02_P1.00mm_Vertical, F.Cu at (192.7, 58.2)
- added J8: Conn_01x02_Pin, Connector_PinHeader_1.00mm:PinHeader_1x02_P1.00mm_Vertical, F.Cu at (205.6, 58.2)
- C1, C2, C3, C4, C5, C6, C7, C8: footprint Capacitor_SMD:C_0603_1608Metric -> Capacitor_SMD:C_0805_2012Metric
- D1, D2, D3, D4, D5, D6, D7, D8: footprint LED_SMD:LED_0805_2012Metric_Pad1.15x1.40mm_HandSolder -> Capacitor_SMD:C_0805_2012Metric
- R1, R11, R13, R15, R3, R5, R7, R9: value 470R -> 360R
- moved C1 3.75 mm to (109.8, 65.9), turned to 0 degrees
- moved C2 3.75 mm to (122.8, 65.9), turned to 0 degrees
- moved C3 3.75 mm to (135.7, 65.9), turned to 0 degrees
- moved C4 3.75 mm to (148.7, 65.9), turned to 0 degrees
- moved C5 3.75 mm to (161.6, 65.9), turned to 0 degrees
- moved C6 3.75 mm to (174.5, 65.9), turned to 0 degrees
- moved C7 3.75 mm to (187.4, 65.9), turned to 0 degrees
- moved C8 3.75 mm to (200.3, 65.9), turned to 0 degrees
- moved Q5 0.30 mm to (110.3, 63.1)
- moved Q14 0.30 mm to (123.2, 63.1)
- moved Q23 0.30 mm to (136.2, 63.1)
- moved Q32 0.30 mm to (149.1, 63.1)
- moved Q41 0.30 mm to (162.0, 63.1)
- moved Q50 0.30 mm to (175.0, 63.1)
- moved Q59 0.30 mm to (187.9, 63.1)
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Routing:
- net GND: track 75.6 -> 50.0 mm, vias 16 -> 24
- net /WL: track 215.6 -> 229.3 mm
- net +5V: track 58.9 -> 66.4 mm
- net Net-(J3-Pin_2): track 23.4 -> 29.8 mm
- net Net-(J5-Pin_2): track 23.4 -> 29.8 mm
- net Net-(J6-Pin_2): track 23.4 -> 29.8 mm
- net Net-(J8-Pin_2): track 23.4 -> 29.8 mm
- net Net-(J4-Pin_2): track 23.4 -> 29.8 mm
- net Net-(J2-Pin_2): track 23.4 -> 29.8 mm
- net Net-(J1-Pin_2): track 23.4 -> 29.8 mm
- net Net-(J7-Pin_2): track 23.4 -> 29.8 mm
- net Net-(J3-Pin_1): track 18.2 -> 23.9 mm
- net Net-(J5-Pin_1): track 18.2 -> 23.9 mm
- net Net-(J7-Pin_1): track 18.2 -> 23.9 mm
- net Net-(J8-Pin_1): track 18.2 -> 23.9 mm
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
